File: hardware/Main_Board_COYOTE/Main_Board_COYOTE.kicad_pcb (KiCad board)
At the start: 2 copper layers, 14 parts, among them J1 FTDI, SW1 SW_SPST, U2 ESP32-WROOM-32, U3 AMS1117-3.3

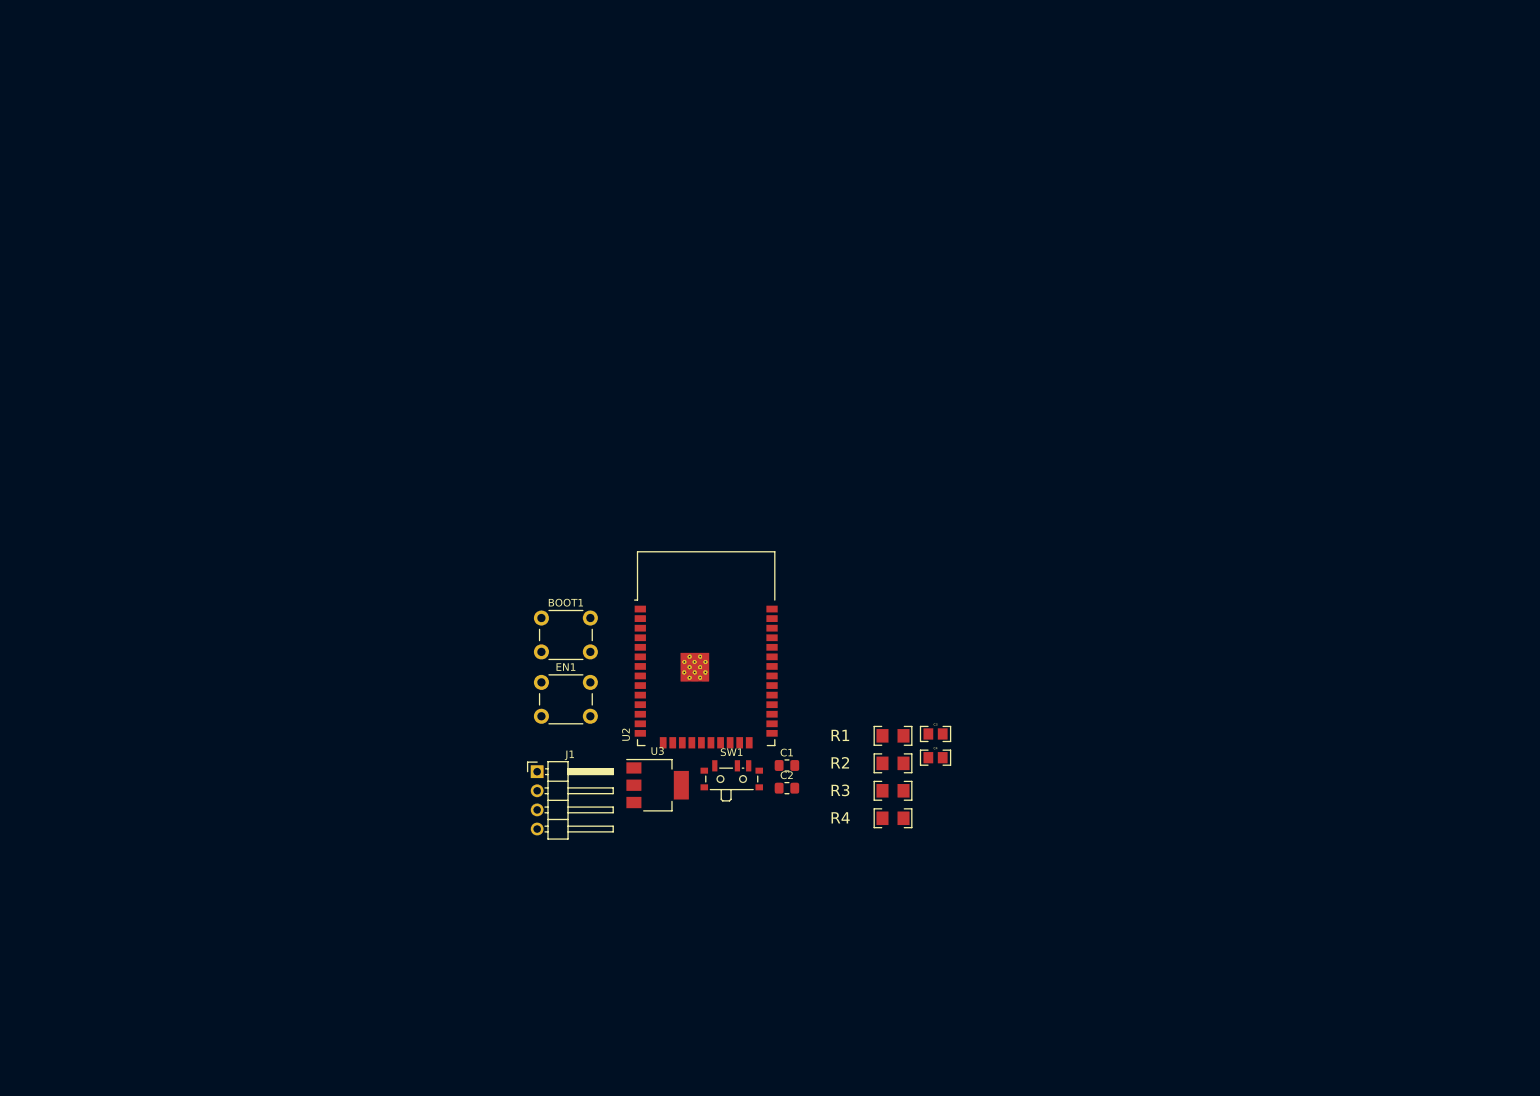
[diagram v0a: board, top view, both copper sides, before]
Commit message: Creacion croquis Velocista
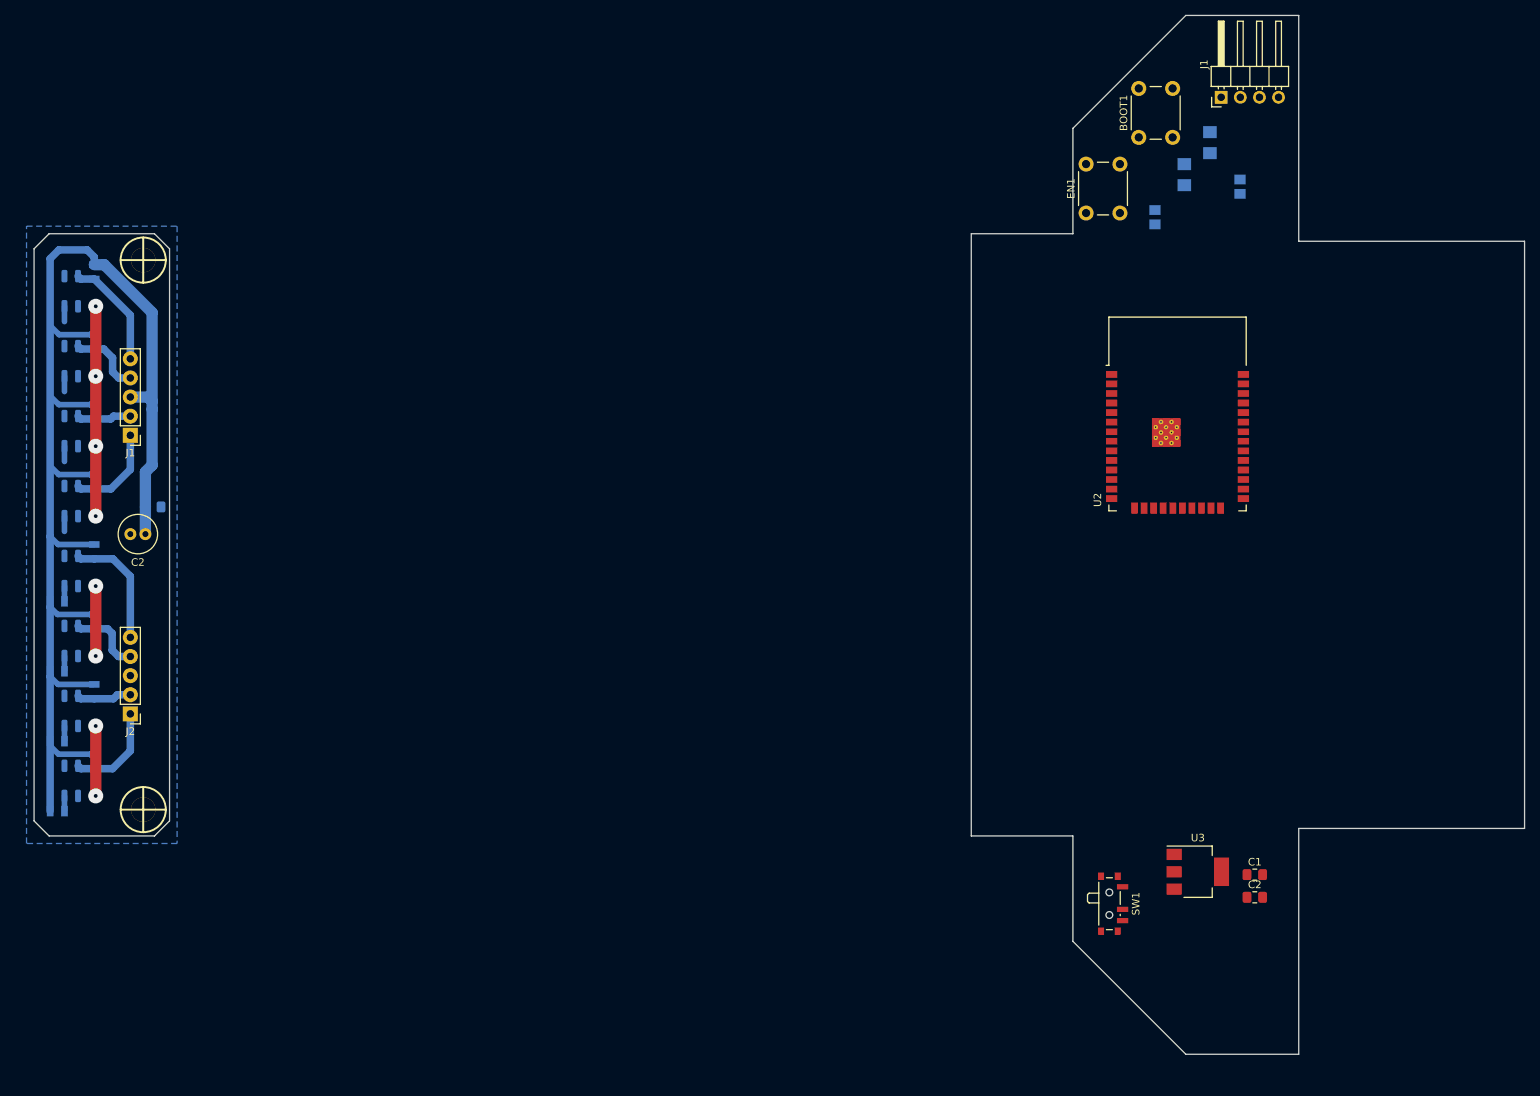
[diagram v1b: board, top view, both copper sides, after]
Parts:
- removed R1, R3: 470, EESTN5-v2:R_1206
- added C1: 100nf, Capacitor_SMD:C_0805_2012Metric_Pad1.18x1.45mm_HandSolder, B.Cu at (68.8, 85.8)
- added C2: 100uf, Capacitor_THT:C_Radial_D5.0mm_H11.0mm_P2.00mm, F.Cu at (67.7, 89.4)
- added H1: HOLE, EESTN5-v2:Separador_M3_5mm, F.Cu at (67.5, 126.0)
- added H2: HOLE, EESTN5-v2:Separador_M3_5mm, F.Cu at (67.5, 53.0)
- added J1: Conn_01x05_Pin, Connector_PinHeader_2.54mm:PinHeader_1x05_P2.54mm_Vertical, F.Cu at (65.7, 76.3)
- added J2: Conn_01x05_Pin, Connector_PinHeader_2.54mm:PinHeader_1x05_P2.54mm_Vertical, F.Cu at (65.7, 113.3)
- added R10: 100, EESTN5-v2:R_0805, B.Cu at (56.0, 107.6)
- added R11: 100, EESTN5-v2:R_0805, B.Cu at (56.0, 116.9)
- added R12: 100, EESTN5-v2:R_0805, B.Cu at (56.0, 126.2)
- added R13: 10k, EESTN5-v2:R_0805, B.Cu at (61.0, 91.7)
- added R14: 10k, EESTN5-v2:R_0805, B.Cu at (61.0, 101.0)
- added R15: 10k, EESTN5-v2:R_0805, B.Cu at (61.0, 110.3)
- added R16: 10k, EESTN5-v2:R_0805, B.Cu at (61.0, 119.6)
- added R5: 10k, EESTN5-v2:R_0805, B.Cu at (61.0, 54.6)
- added R6: 10k, EESTN5-v2:R_0805, B.Cu at (61.0, 63.9)
- added R7: 10k, EESTN5-v2:R_0805, B.Cu at (61.0, 73.2)
- added R8: 10k, EESTN5-v2:R_0805, B.Cu at (61.0, 82.4)
- added R9: 100, EESTN5-v2:R_0805, B.Cu at (56.0, 98.3)
- added U1: QRE1113GR, OptoDevice:OnSemi_CASE100CY, B.Cu at (57.9, 57.1)
- added U2: QRE1113GR, OptoDevice:OnSemi_CASE100CY, B.Cu at (57.9, 66.4)
- added U3: QRE1113GR, OptoDevice:OnSemi_CASE100CY, B.Cu at (57.9, 75.7)
- added U4: QRE1113GR, OptoDevice:OnSemi_CASE100CY, B.Cu at (57.9, 85.0)
- added U5: QRE1113GR, OptoDevice:OnSemi_CASE100CY, B.Cu at (57.9, 94.3)
- added U6: QRE1113GR, OptoDevice:OnSemi_CASE100CY, B.Cu at (57.9, 103.6)
- added U7: QRE1113GR, OptoDevice:OnSemi_CASE100CY, B.Cu at (57.9, 112.9)
- added U8: QRE1113GR, OptoDevice:OnSemi_CASE100CY, B.Cu at (57.9, 122.2)
- C3, C4, R2, R4: moved to B.Cu
- moved J1 127.6 mm to (210.7, 31.4), turned to 90 degrees
- moved BOOT1 101.8 mm to (199.7, 36.7), turned to 90 degrees
- moved R4 99.1 mm to (209.2, 37.4), turned to 90 degrees
- moved EN1 95.5 mm to (192.7, 46.8), turned to 90 degrees
- moved R2 87.2 mm to (205.8, 41.7), turned to -90 degrees
- moved C4 86.0 mm to (213.2, 43.2), turned to 90 degrees
- moved C3 74.6 mm to (201.8, 47.3), turned to -90 degrees
- moved U3 72.7 mm to (207.6, 134.2)
- moved U2 70.0 mm to (204.8, 76.4)
- moved C1 63.8 mm to (215.1, 134.6)
- moved C2 63.8 mm to (215.1, 137.7)
- moved SW1 53.2 mm to (196.1, 138.5), turned to -90 degrees
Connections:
- BOOT1 pad 2: Net-(BOOT1-Pad2) -> /IO0
- C3 pad 2: Net-(BOOT1-Pad2) -> /IO0
- C4 pad 2: Net-(C4-Pad2) -> /EN
- EN1 pad 2: Net-(C4-Pad2) -> /EN
- U2 pad 25: unconnected-(U2-IO0-Pad25) -> /IO0
- U2 pad 3: unconnected-(U2-EN-Pad3) -> /EN
- U2 pad 34: unconnected-(U2-RXD0/IO3-Pad34) -> /Tx
- U2 pad 35: unconnected-(U2-TXD0/IO1-Pad35) -> /Rx
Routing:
- net +3V3: track 0.00 -> 170.8 mm
- net (no net): track 0.00 -> 107.4 mm
- net GND: track 0.00 -> 46.5 mm, vias 0 -> 8
- added copper zone on B.Cu, net GND
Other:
- board outline added: 198 x 138 mm

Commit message: Creacion finalizacion del croquis velocista
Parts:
- added BZ1: Buzzer, EESTN5-v2:Buzzer_12mm, F.Cu at (203.9, 65.7)
- added J2: Conn_01x05_Pin, Connector_PinHeader_2.54mm:PinHeader_1x05_P2.54mm_Horizontal, F.Cu at (188.2, 113.3)
- added J3: Conn_01x05_Pin, Connector_PinHeader_2.54mm:PinHeader_1x05_P2.54mm_Horizontal, F.Cu at (188.2, 76.3)
- added Q1: 2N7002, Package_TO_SOT_SMD:SOT-23, B.Cu at (208.4, 68.3)
- added R1: 4K7, EESTN5-v2:R_1206, B.Cu at (214.4, 120.5)
- added R3: 4K7, EESTN5-v2:R_1206, B.Cu at (214.4, 111.9)
- added R5: 10K, EESTN5-v2:R_1206, B.Cu at (207.8, 64.2)
- added SW2: START, Button_Switch_THT:SW_PUSH_6mm_H5mm, F.Cu at (203.6, 124.7)
- added SW3: START, Button_Switch_THT:SW_PUSH_6mm_H5mm, F.Cu at (203.6, 116.1)
- moved C4 20.8 mm to (193.5, 50.0), turned to 180 degrees
- moved R4 20.5 mm to (195.9, 53.0), turned to 180 degrees
- moved U2 17.8 mm to (210.5, 93.3)
- moved C3 8.56 mm to (201.6, 38.8), turned to 180 degrees
- moved R2 1.77 mm to (204.0, 41.8), turned to 180 degrees
- moved BOOT1 1.55 mm to (200.7, 35.5)
- moved J1 0.66 mm to (210.0, 31.1)
- moved EN1 0.12 mm to (192.6, 46.8)
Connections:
- C2 pad 1: +3.3V -> +3V3
- J1 pad 2: +3.3V -> +3V3
- U2 pad 1: Net-(U2-GND-Pad1) -> GND
- U2 pad 10: unconnected-(U2-IO25-Pad10) -> /OUT_5
- U2 pad 11: unconnected-(U2-IO26-Pad11) -> /OUT_6
- U2 pad 12: unconnected-(U2-IO27-Pad12) -> /OUT_7
- U2 pad 15: Net-(U2-GND-Pad1) -> GND
- U2 pad 16: unconnected-(U2-IO13-Pad16) -> /OUT_8
- U2 pad 2: +3.3V -> +3V3
- U2 pad 24: unconnected-(U2-IO2-Pad24) -> /LED_BUILTING
- U2 pad 25: /IO0 -> /BOOT
- U2 pad 26: unconnected-(U2-IO4-Pad26) -> /LED_1
- U2 pad 27: unconnected-(U2-IO16-Pad27) -> /PUSH_1
- U2 pad 28: unconnected-(U2-IO17-Pad28) -> /PUSH_2
- U2 pad 29: unconnected-(U2-IO5-Pad29) -> /LED_2
- U2 pad 30: unconnected-(U2-IO18-Pad30) -> /BUZZER
- U2 pad 31: unconnected-(U2-IO19-Pad31) -> /M1A
- U2 pad 33: unconnected-(U2-IO21-Pad33) -> /M1B
- U2 pad 36: unconnected-(U2-IO22-Pad36) -> /M2A
- U2 pad 37: unconnected-(U2-IO23-Pad37) -> /M2B
- U2 pad 38: Net-(U2-GND-Pad1) -> GND
- U2 pad 39: Net-(U2-GND-Pad1) -> GND
- U2 pad 6: unconnected-(U2-IO34-Pad6) -> /OUT_1
- U2 pad 7: unconnected-(U2-IO35-Pad7) -> /OUT_2
- U2 pad 8: unconnected-(U2-IO32-Pad8) -> /OUT_3
- U2 pad 9: unconnected-(U2-IO33-Pad9) -> /OUT_4
- U3 pad 2: +3.3V -> +3V3
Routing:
- net GND: track 46.5 -> 135.8 mm
- net +3V3: track 170.8 -> 241.2 mm, vias 0 -> 1
- net /EN: track 0.00 -> 56.0 mm, vias 0 -> 1
- net /OUT_1: track 0.00 -> 34.9 mm
- net /OUT_2: track 0.00 -> 34.2 mm
- net /OUT_3: track 0.00 -> 30.9 mm
- net /OUT_4: track 0.00 -> 30.1 mm
- net /OUT_8: track 0.00 -> 23.8 mm
- net /OUT_7: track 0.00 -> 21.5 mm
- net /OUT_6: track 0.00 -> 18.7 mm
- net /OUT_5: track 0.00 -> 18.0 mm
- net /IO0: track 0.00 -> 14.3 mm
- net /Tx: track 0.00 -> 5.34 mm, vias 0 -> 1
- net /Rx: track 0.00 -> 5.28 mm, vias 0 -> 1

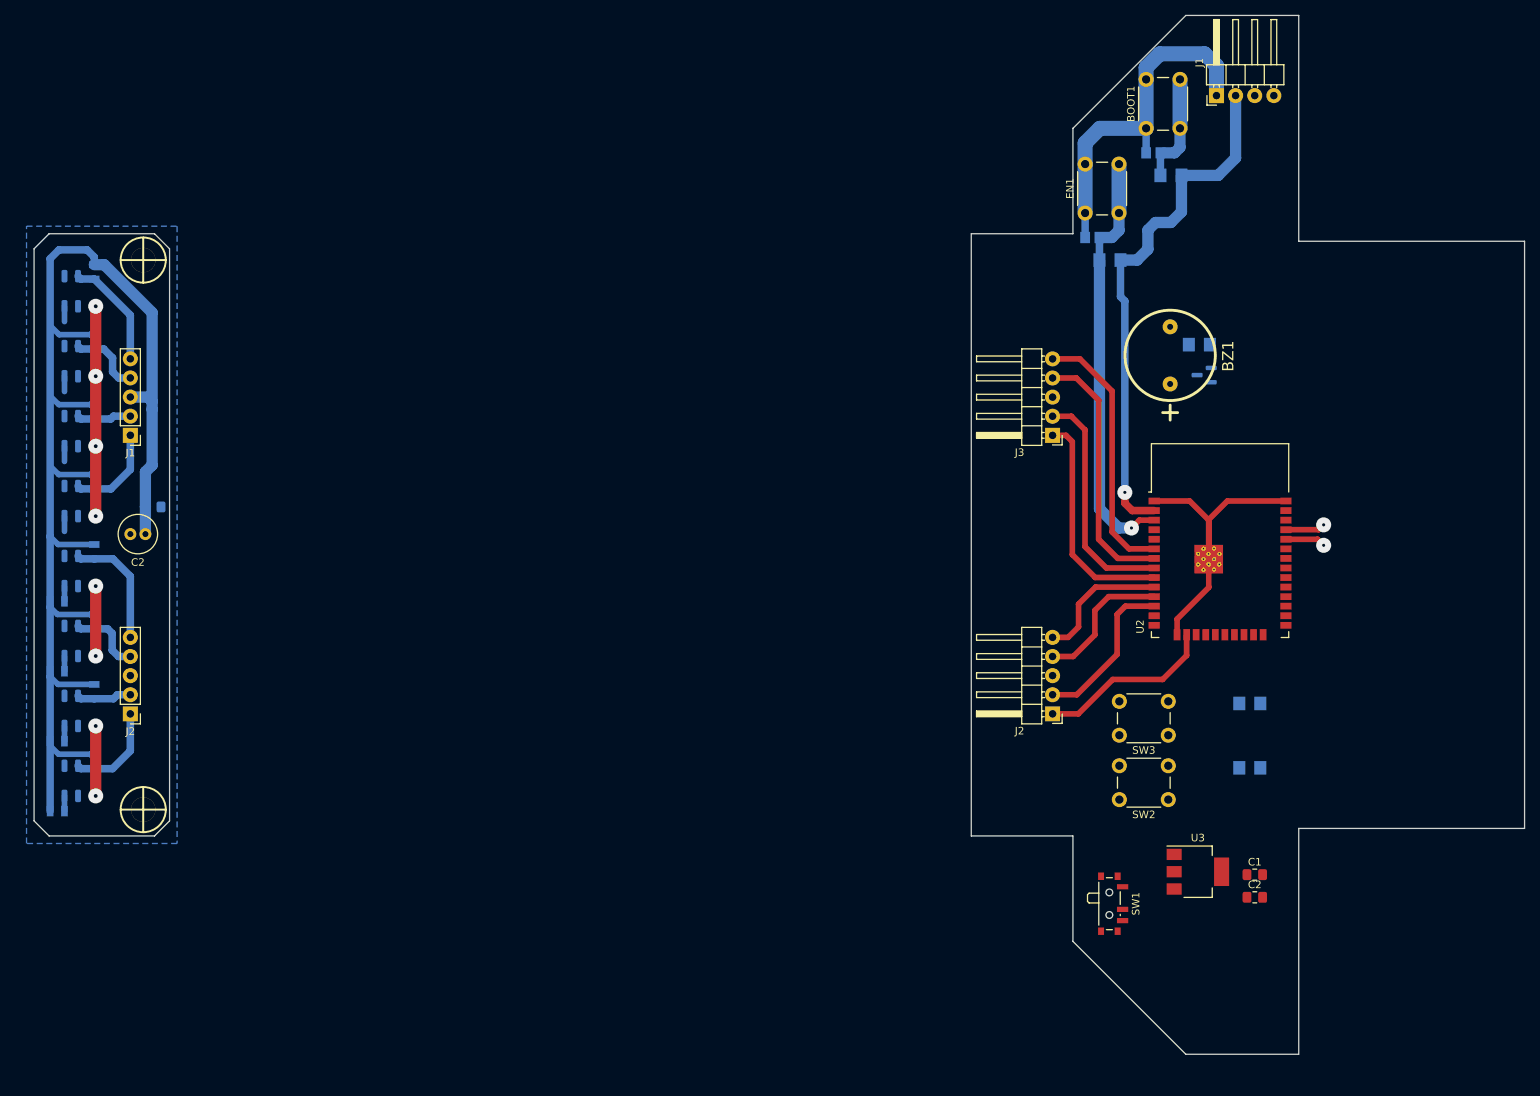
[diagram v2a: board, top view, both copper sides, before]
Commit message: Edicion SCh y PCB de la main board
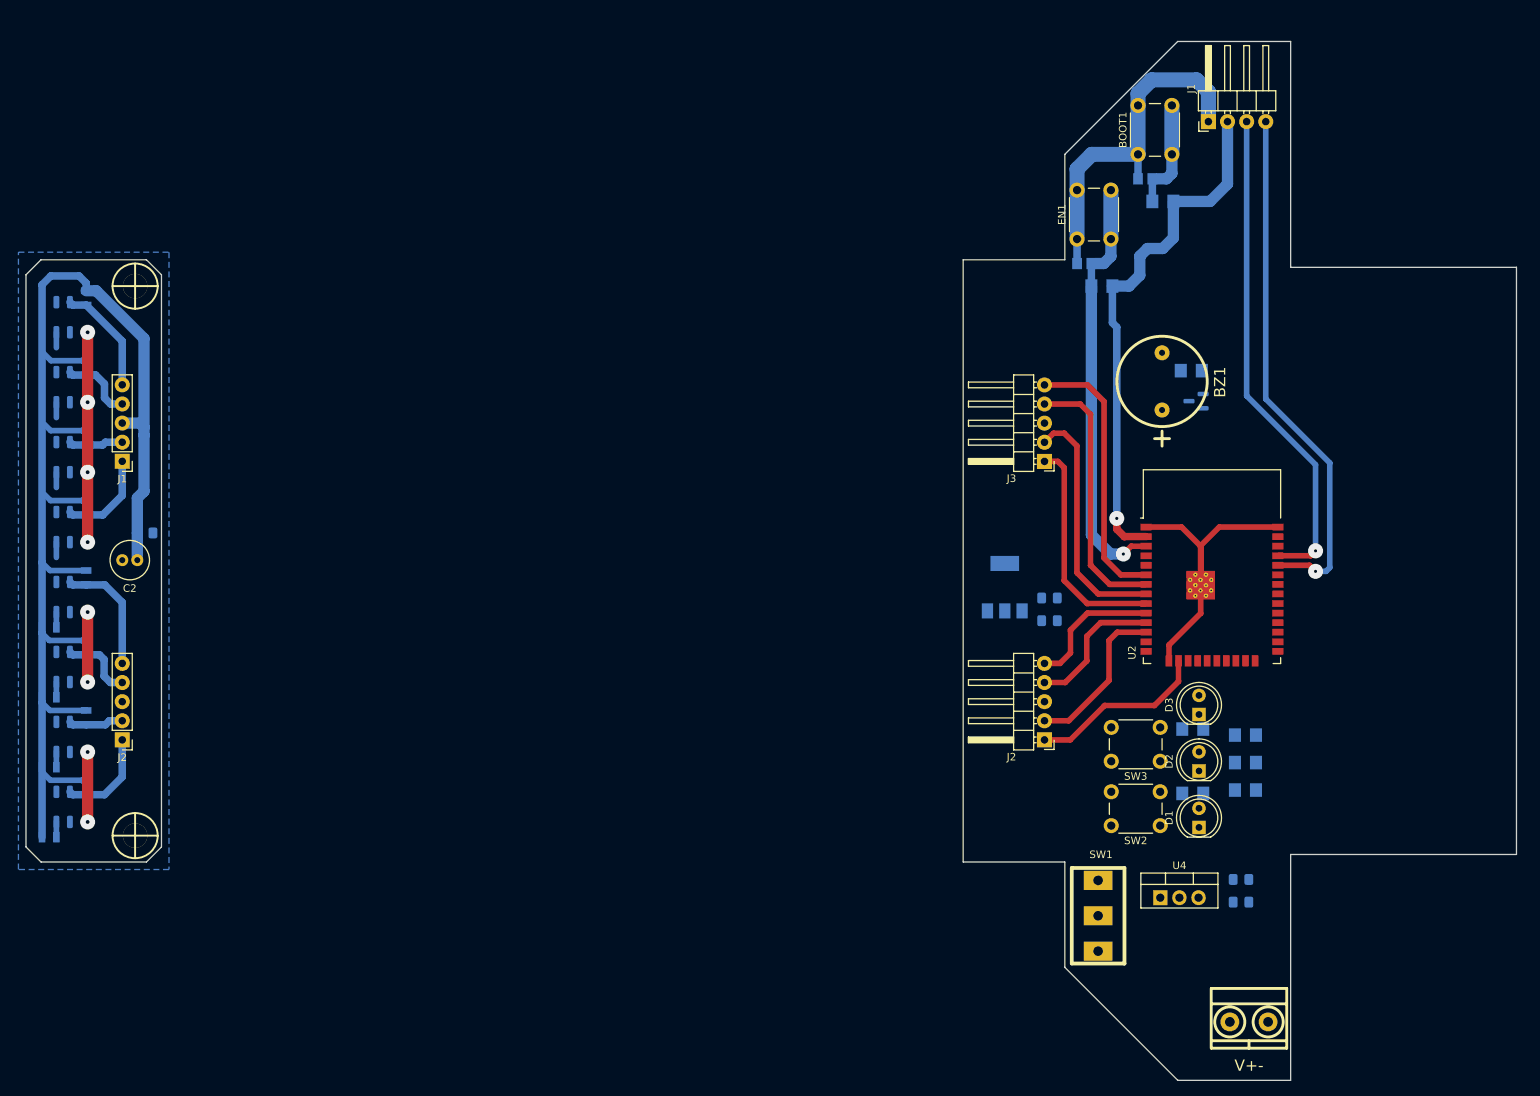
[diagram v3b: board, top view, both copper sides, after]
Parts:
- added C5: 1uF, Capacitor_SMD:C_0805_2012Metric_Pad1.18x1.45mm_HandSolder, B.Cu at (213.3, 135.3)
- added C8: 1uF, Capacitor_SMD:C_0805_2012Metric_Pad1.18x1.45mm_HandSolder, B.Cu at (213.3, 138.3)
- added D1: LED, LED_THT:LED_D5.0mm, F.Cu at (207.7, 128.4)
- added D2: LED, LED_THT:LED_D5.0mm, F.Cu at (207.7, 120.9)
- added D3: LED, LED_THT:LED_D5.0mm, F.Cu at (207.7, 113.4)
- added J4: V+-, EESTN5-v2:BORNERA2_AZUL, F.Cu at (214.3, 154.2)
- added R6: 220, EESTN5-v2:R_1206, B.Cu at (213.9, 123.4)
- added R7: 220, EESTN5-v2:R_1206, B.Cu at (213.9, 119.8)
- added R8: 220, EESTN5-v2:R_1206, B.Cu at (213.9, 116.1)
- added U4: LM7805_TO220, Package_TO_SOT_THT:TO-220-3_Vertical, F.Cu at (202.6, 137.7)
- C1, C2, U3: moved to B.Cu
- SW1: footprint Button_Switch_SMD:SW_SPDT_PCM12 -> EESTN5-v2:SW_SPDT_TH_Vertical
- moved C2 45.8 mm to (187.8, 100.9), turned to 180 degrees
- moved C1 45.8 mm to (187.8, 97.9), turned to 180 degrees
- moved U3 45.7 mm to (181.9, 96.5), turned to 90 degrees
- moved R1 8.30 mm to (206.9, 123.8)
- moved R3 8.30 mm to (206.9, 115.3)
- moved BZ1 3.62 mm to (202.8, 69.1)
- moved H1 3.62 mm to (66.4, 129.5)
- moved R11 3.62 mm to (55.0, 120.4)
- moved R13 3.62 mm to (59.9, 95.2)
- moved U4 3.62 mm to (56.8, 88.5)
- moved U6 3.62 mm to (56.8, 107.1)
- moved C4 3.62 mm to (192.5, 53.5)
- moved J1 3.62 mm to (208.9, 34.6)
- moved R2 3.62 mm to (202.9, 45.2)
- moved R4 3.62 mm to (194.8, 56.5)
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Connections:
- BOOT1 pad 2: /IO0 -> /BOOT
- C3 pad 2: /IO0 -> /BOOT
- R2 pad 1: /IO0 -> /BOOT
- SW1 pad 1: /VBAT -> VCC
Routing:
- net /Tx: track 5.34 -> 70.2 mm
- net /Rx: track 5.28 -> 66.1 mm
- net /IO0: track 14.3 -> 0.00 mm
- net /BOOT: track 0.00 -> 14.3 mm
- net /OUT_3: track 30.9 -> 32.7 mm
- net /OUT_1: track 34.9 -> 36.1 mm
- net /OUT_2: track 34.2 -> 35.2 mm
